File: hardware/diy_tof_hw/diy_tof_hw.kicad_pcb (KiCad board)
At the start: 2 copper layers, 100 x 100 mm, 69 parts, among them IC1 TDC7200PWR, IC2 TDC7200PWR, IC21 74LVC1G08QW5-7, IC22 LMG1025QDEETQ1, J1 Conn_01x02_Pin, J2 Conn_01x03_Pin, J3 Conn_01x02_Pin, SW1 SW_Nidec_CAS-120A1, SW2 SW_Nidec_CAS-120A1, U1 NUCLEO-F042K6, U2 OPA858xDSG, U3 TLV3501AIDBV, X1 SG-5032CAN

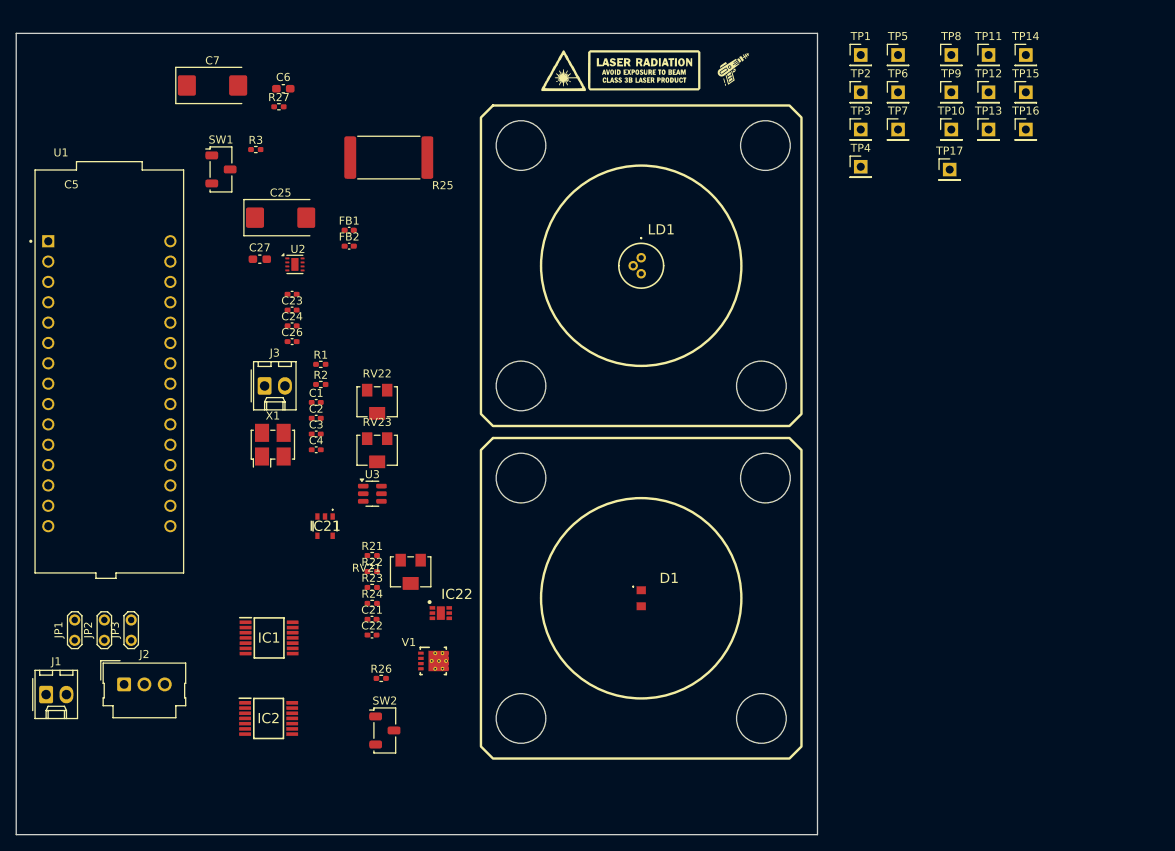
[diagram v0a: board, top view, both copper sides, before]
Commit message: [hardware] added mounting holes, reannotated some caps, started placement of the TIA part
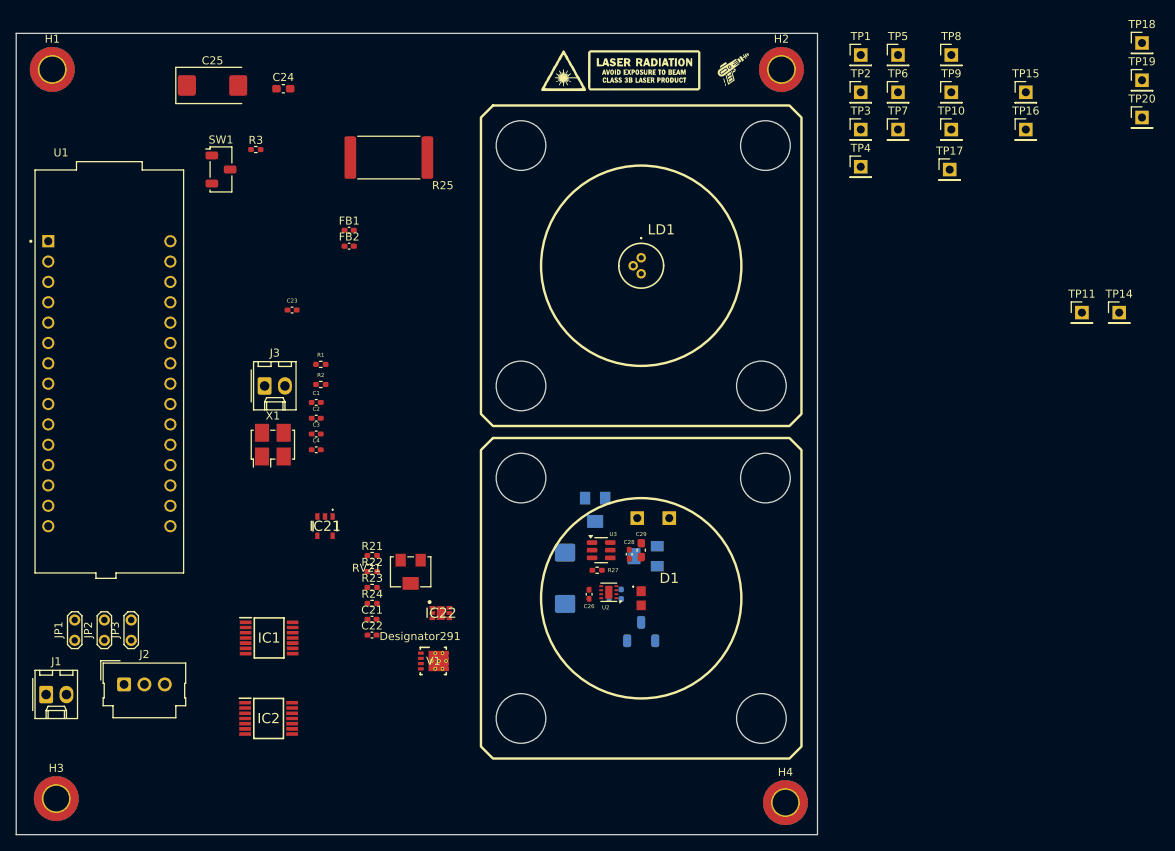
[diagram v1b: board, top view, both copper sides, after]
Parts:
- added H1: MountingHole_Pad, MountingHole:MountingHole_3.2mm_M3_DIN965_Pad_TopBottom, F.Cu at (50.5, 34.5)
- added H2: MountingHole_Pad, MountingHole:MountingHole_3.2mm_M3_DIN965_Pad_TopBottom, F.Cu at (141.5, 34.5)
- added H3: MountingHole_Pad, MountingHole:MountingHole_3.2mm_M3_DIN965_Pad_TopBottom, F.Cu at (51.0, 125.5)
- added H4: MountingHole_Pad, MountingHole:MountingHole_3.2mm_M3_DIN965_Pad_TopBottom, F.Cu at (142.0, 126.0)
- added TP18: Conn_01x01_Pin, Connector_PinHeader_2.54mm:PinHeader_1x01_P2.54mm_Vertical, F.Cu at (186.5, 31.2)
- added TP19: Conn_01x01_Pin, Connector_PinHeader_2.54mm:PinHeader_1x01_P2.54mm_Vertical, F.Cu at (186.5, 35.9)
- added TP20: Conn_01x01_Pin, Connector_PinHeader_2.54mm:PinHeader_1x01_P2.54mm_Vertical, F.Cu at (186.5, 40.5)
- C20: renamed from C5; moved to B.Cu
- C27: renamed from C25; moved to B.Cu
- R26, RV22, RV23, SW2, TP12, TP13: moved to B.Cu
- moved R27 70.2 mm to (118.5, 97.0), turned to 180 degrees
- moved TP12 68.9 mm to (123.5, 90.5), turned to 180 degrees
- moved TP13 62.8 mm to (127.5, 90.5), turned to 180 degrees
- moved C29 59.9 mm to (124.0, 94.5), turned to 90 degrees
- moved C27 57.3 mm to (114.5, 98.0), turned to 90 degrees
- moved U2 56.6 mm to (120.0, 99.8), turned to 180 degrees
- moved C20 54.5 mm to (120.0, 100.0), turned to -90 degrees
- moved C26 50.0 mm to (117.5, 100.0), turned to 90 degrees
- moved C28 49.7 mm to (122.5, 95.0), turned to 90 degrees
- moved X2 41.5 mm to (124.0, 100.5)
- moved X3 41.5 mm to (124.0, 59.0)
- moved RV22 38.7 mm to (124.5, 95.2), turned to 90 degrees
- moved SW2 34.3 mm to (124.0, 104.7), turned to 90 degrees
- moved TP11 34.2 mm to (179.0, 64.8)
- moved TP14 34.2 mm to (183.7, 64.8)
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- renumbered C6 to C24, C7 to C25, C24 to C26, C26 to C28, C27 to C29

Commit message: [hardware] placed all components, some minor renaming (got rid of the "+" in front of all source-labels)
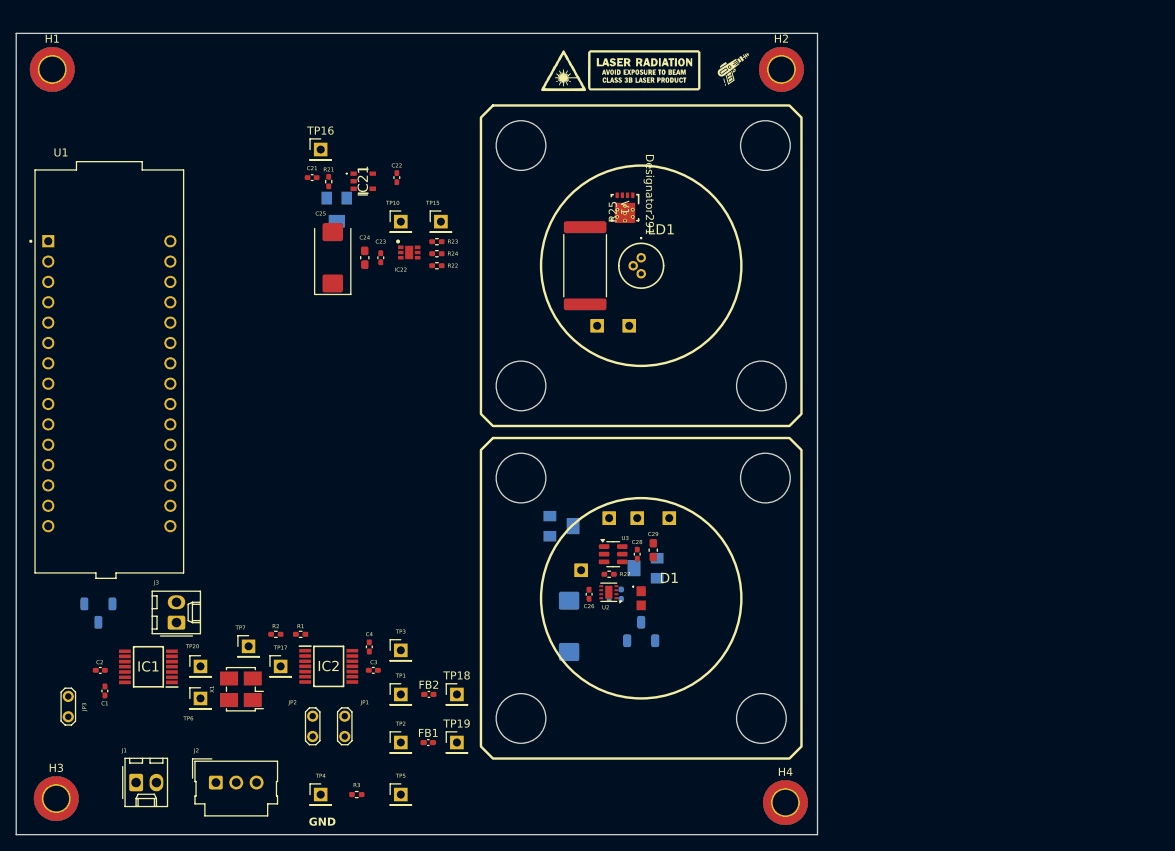
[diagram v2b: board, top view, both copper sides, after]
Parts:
- RV21, SW1, TP11, TP14, TP8, TP9: moved to B.Cu
- moved TP20 136.0 mm to (69.0, 109.0)
- moved TP19 118.9 mm to (101.0, 118.5)
- moved TP18 118.0 mm to (101.0, 112.5)
- moved TP6 115.3 mm to (69.0, 113.0)
- moved TP5 111.2 mm to (94.0, 125.0)
- moved TP17 104.0 mm to (79.0, 109.0)
- moved TP7 103.6 mm to (75.0, 106.5)
- moved TP4 103.4 mm to (84.0, 125.0)
- moved TP2 99.4 mm to (94.0, 118.5)
- moved TP1 98.3 mm to (94.0, 112.5)
- moved TP16 88.0 mm to (84.0, 44.5)
- moved TP3 86.7 mm to (94.0, 107.0)
- moved R3 81.5 mm to (88.5, 125.0)
- moved TP15 74.8 mm to (99.0, 53.5)
- moved TP11 70.3 mm to (116.5, 97.0), turned to 180 degrees
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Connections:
- net +12V renamed 12V
- net +5V_ext renamed 5V_ext
- net +5V_nuc renamed 5V_nuc
- TP19 pad 1: +12V_LN -> 12V_LN
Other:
- board text added: "GND"

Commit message: [hardware] initial version of the PCB layout
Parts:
- moved C1 42.1 mm to (73.0, 73.1), turned to 180 degrees
- moved C2 41.6 mm to (75.5, 72.5), turned to 90 degrees
- moved SW1 40.1 mm to (82.7, 72.2), turned to 180 degrees
- moved IC1 33.4 mm to (76.0, 78.5), turned to 90 degrees
- moved JP1 31.3 mm to (57.0, 108.8), turned to -90 degrees
- moved TP6 28.2 mm to (72.0, 85.0), turned to -90 degrees
- moved J3 26.5 mm to (81.5, 82.0), turned to 0 degrees
- moved JP2 26.0 mm to (57.0, 117.2)
- moved TP16 25.1 mm to (73.0, 67.1)
- moved TP20 25.0 mm to (76.0, 85.0), turned to -90 degrees
- moved X1 22.3 mm to (78.3, 89.9), turned to 180 degrees
- moved C21 18.6 mm to (74.6, 64.6)
- moved C22 18.6 mm to (85.1, 64.6)
- moved IC21 18.6 mm to (80.9, 65.1)
- moved R21 18.6 mm to (76.6, 65.1)
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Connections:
- V1 pad 9: (no net) -> Net-(LD1-Pad1)
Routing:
- net /Power_Nucleo_TDC/12_nuc: track 0.00 -> 71.2 mm
- net /Power_Nucleo_TDC/int_opt: track 0.00 -> 68.4 mm, vias 0 -> 2
- net /Power_Nucleo_TDC/spi_mosi: track 0.00 -> 57.7 mm, vias 0 -> 4
- net /Power_Nucleo_TDC/spi_miso: track 0.00 -> 56.9 mm, vias 0 -> 4
- net /Power_Nucleo_TDC/spi_cs_opt: track 0.00 -> 56.3 mm, vias 0 -> 2
- net /Power_Nucleo_TDC/stop_ele: track 0.00 -> 52.3 mm, vias 0 -> 2
- net /Power_Nucleo_TDC/start_opt: track 0.00 -> 52.3 mm, vias 0 -> 2
- net 5V_nuc: track 0.00 -> 48.6 mm
- net /Power_Nucleo_TDC/int_ele: track 0.00 -> 47.2 mm, vias 0 -> 3
- net /Optoelectronics/~{LD_enable}: track 0.00 -> 42.3 mm, vias 0 -> 2
- net /Power_Nucleo_TDC/start_ele: track 0.00 -> 40.6 mm, vias 0 -> 2
- net /Optoelectronics/LD_pulse: track 0.00 -> 38.9 mm, vias 0 -> 2
- net /Power_Nucleo_TDC/spi_clk: track 0.00 -> 38.7 mm, vias 0 -> 3
- net /Optoelectronics/stop_opt: track 0.00 -> 36.4 mm, vias 0 -> 2
- net 12V: track 0.00 -> 31.5 mm
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- added copper zone on F.Cu, net 12V_LN
- added copper zone on F.Cu, net 3V3
- added copper zone on F.Cu, net 5V
- added copper zone on F.Cu, net 5V_LN
- added copper zone on B.Cu, net GND
- added copper zone on B.Cu, net GNDA
- added copper zone on F.Cu, net GNDA
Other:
- board size 100 x 100 mm -> 90 x 100 mm
- copper layers 2 -> 4
- board text added: "12V"
- board text added: "3V3"
- board text added: "5V"
